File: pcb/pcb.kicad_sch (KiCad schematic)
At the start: 0 parts

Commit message: Start the schematic for the PCB
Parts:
- added J1: Conn_01x04_Pin, symbol Connector:Conn_01x04_Pin
- added J2: Conn_01x06_Pin, symbol Connector:Conn_01x06_Pin
- added R1, R10, R11, R12, R13, R14, R15, R16, R2, R3, R4, R5, R6, R7, R8, R9: 10k, symbol Device:R
- added U1: XIAO-ESP32-C5-DIP, Seeed_Studio_XIAO_Series:XIAO-ESP32-C5-DIP, symbol XIAO_Symbols:XIAO-ESP32-C5-DIP
- added U16: (no value), symbol esp32_wroom:esp32-s3-devkitc-1
- added U17: AP2112K-3.3, Package_TO_SOT_SMD:SOT-23-5, symbol Regulator_Linear:AP2112K-3.3
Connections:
- new net +5V: U1.14 (VBUS), U16.21 (5V)
- new net GND: U1.13 (GND), U16.22 (GND)
- new net MISO: U1.10 (GPIO9_D9_MISO), U16.19 (GPIO13)
- new net MOSI: U1.11 (GPIO18_D10_MOSI), U16.17 (GPIO11)
- new net SCK: J2.2 (Pin_2), U1.9 (GPIO8_D8_SCK), U16.18 (GPIO12)
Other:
- note added: "3.3V"
- note added: "5V"
- note added: "CS"
- note added: "GND"
- note added: "MISO"
- note added: "MOSI"
- note added: "RX"
- note added: "SCLK"
- note added: "TX"
- title: (none) -> wifydra-spi

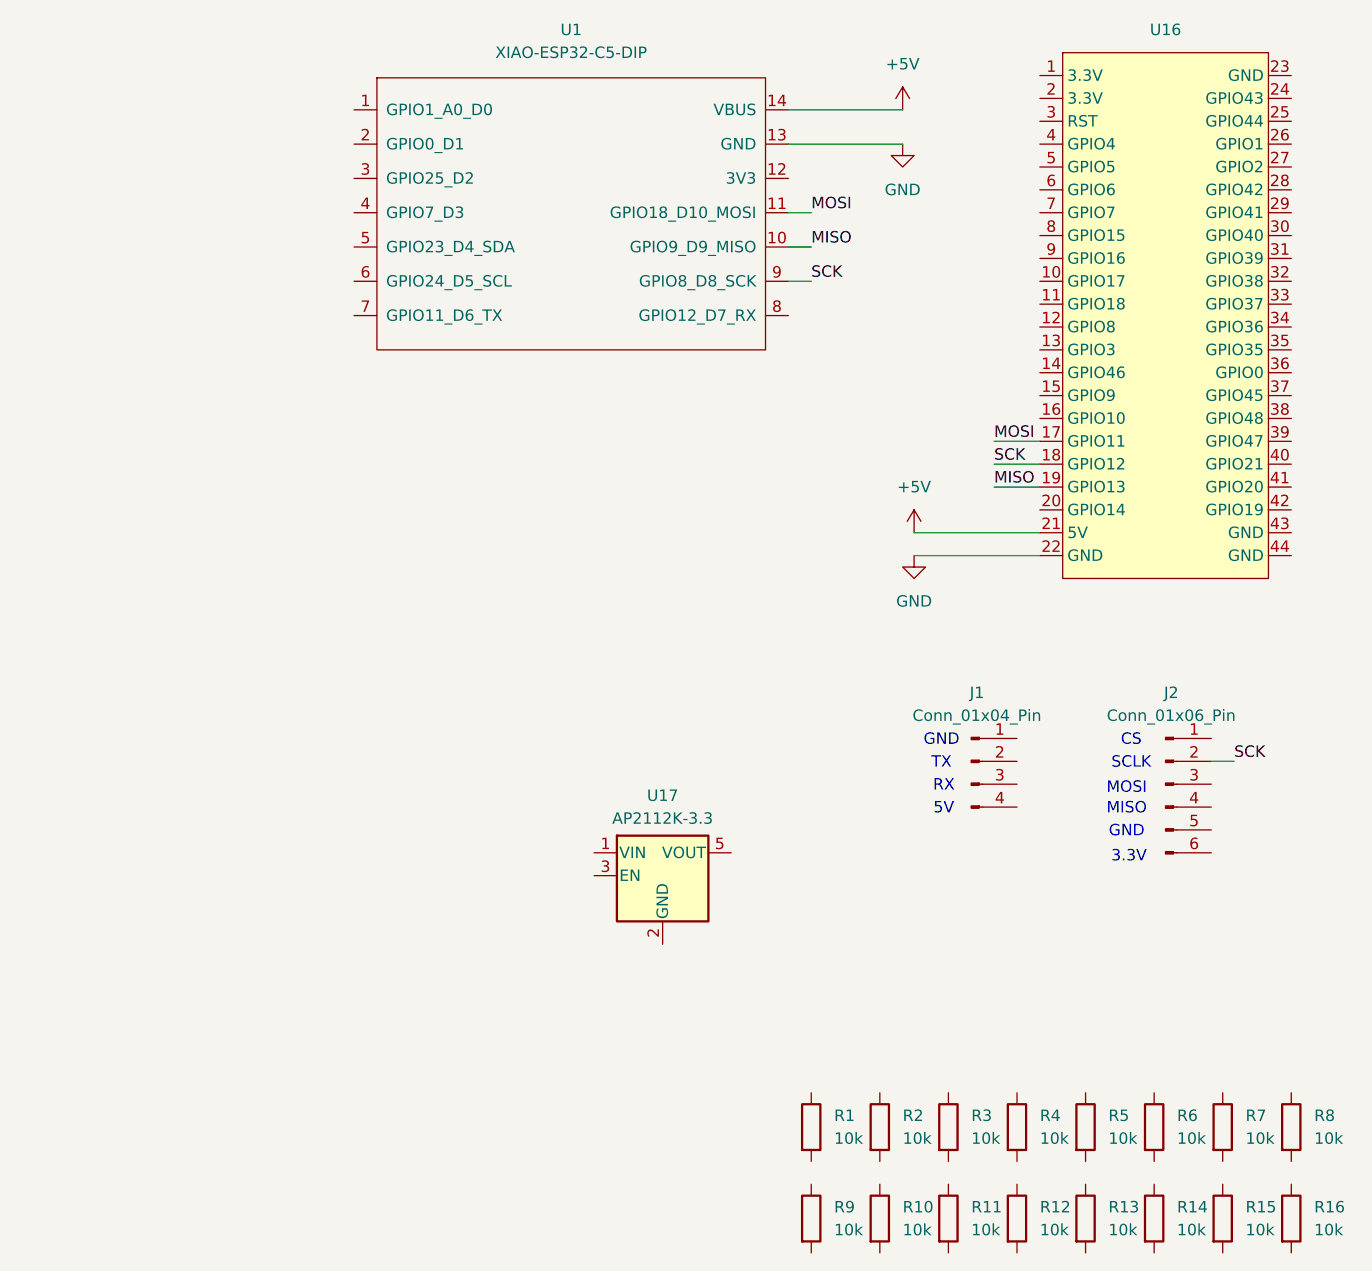
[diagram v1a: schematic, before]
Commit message: More wiring on the PCB design
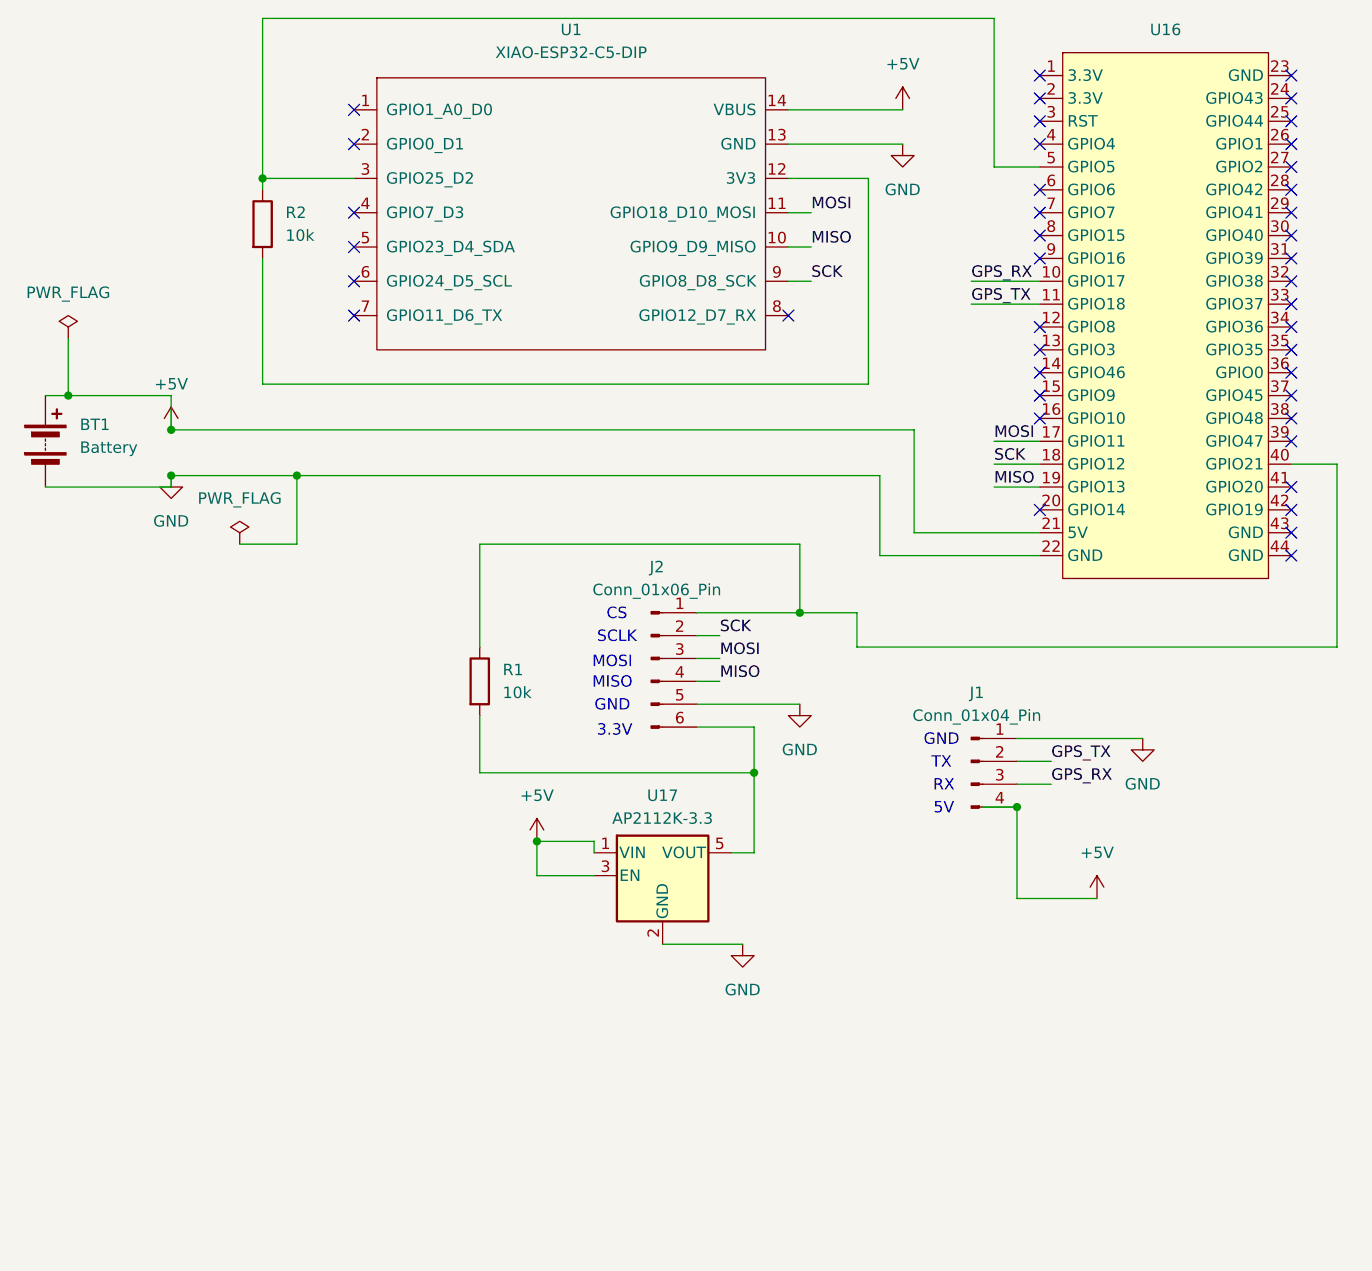
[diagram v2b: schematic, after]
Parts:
- removed R10, R11, R12, R13, R14, R15, R16, R3, R4, R5, R6, R7, R8, R9: 10k, symbol Device:R
- added BT1: Battery, Connector_PinHeader_2.54mm:PinHeader_1x02_P2.54mm_Horizontal, symbol Device:Battery
- J1: footprint (none) -> Connector_PinHeader_2.54mm:PinHeader_1x04_P2.54mm_Horizontal
- J2: footprint (none) -> Connector_PinHeader_2.54mm:PinHeader_1x06_P2.54mm_Vertical
- R1, R2: footprint (none) -> Resistor_THT:R_Axial_DIN0204_L3.6mm_D1.6mm_P5.08mm_Horizontal
- U1: footprint Seeed_Studio_XIAO_Series:XIAO-ESP32-C5-DIP -> xiao_footprints:XIAO-ESP32-C5-DIP
- U16: footprint (none) -> PCM_Espressif:ESP32-S3-DevKitC
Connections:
- net +5V: now also J1.4 (Pin_4), U17.1 (VIN), U17.3 (EN), BT1.1 (+)
- net GND: now also J1.1 (Pin_1), J2.5 (Pin_5), U17.2 (GND), BT1.2 (-)
- net MISO: now also J2.4 (Pin_4)
- net MOSI: now also J2.3 (Pin_3)
- net GPS_TX: now reaches J1.2 (Pin_2)
- net GPS_TX: now also U16.11 (GPIO18)
- net GPS_RX: now reaches J1.3 (Pin_3)
- net GPS_RX: now also U16.10 (GPIO17)
- net at R1.1: now also J2.1 (Pin_1), U16.40 (GPIO21)
- net at R1.2: now also J2.6 (Pin_6), U17.5 (VOUT)
- net at U16.5 (GPIO5): now also R2.1, U1.3 (GPIO25_D2)
- net at R2.2: now also U1.12 (3V3)
- no-connect marks 0 -> 42
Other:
- moved on the sheet: J2, R1, R2

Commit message: tidy schematic
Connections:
- net GND: now also U16.44 (GND)
- net at J2.1 (Pin_1), R1.1, U16.40 (GPIO21): now also J2.6 (Pin_6), R1.2, U17.5 (VOUT)
- net at R2.1, U1.3 (GPIO25_D2), U16.5 (GPIO5): now also R2.2, U1.12 (3V3)
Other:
- moved on the sheet: BT1, J2, R1, R2, U1, U16, U17

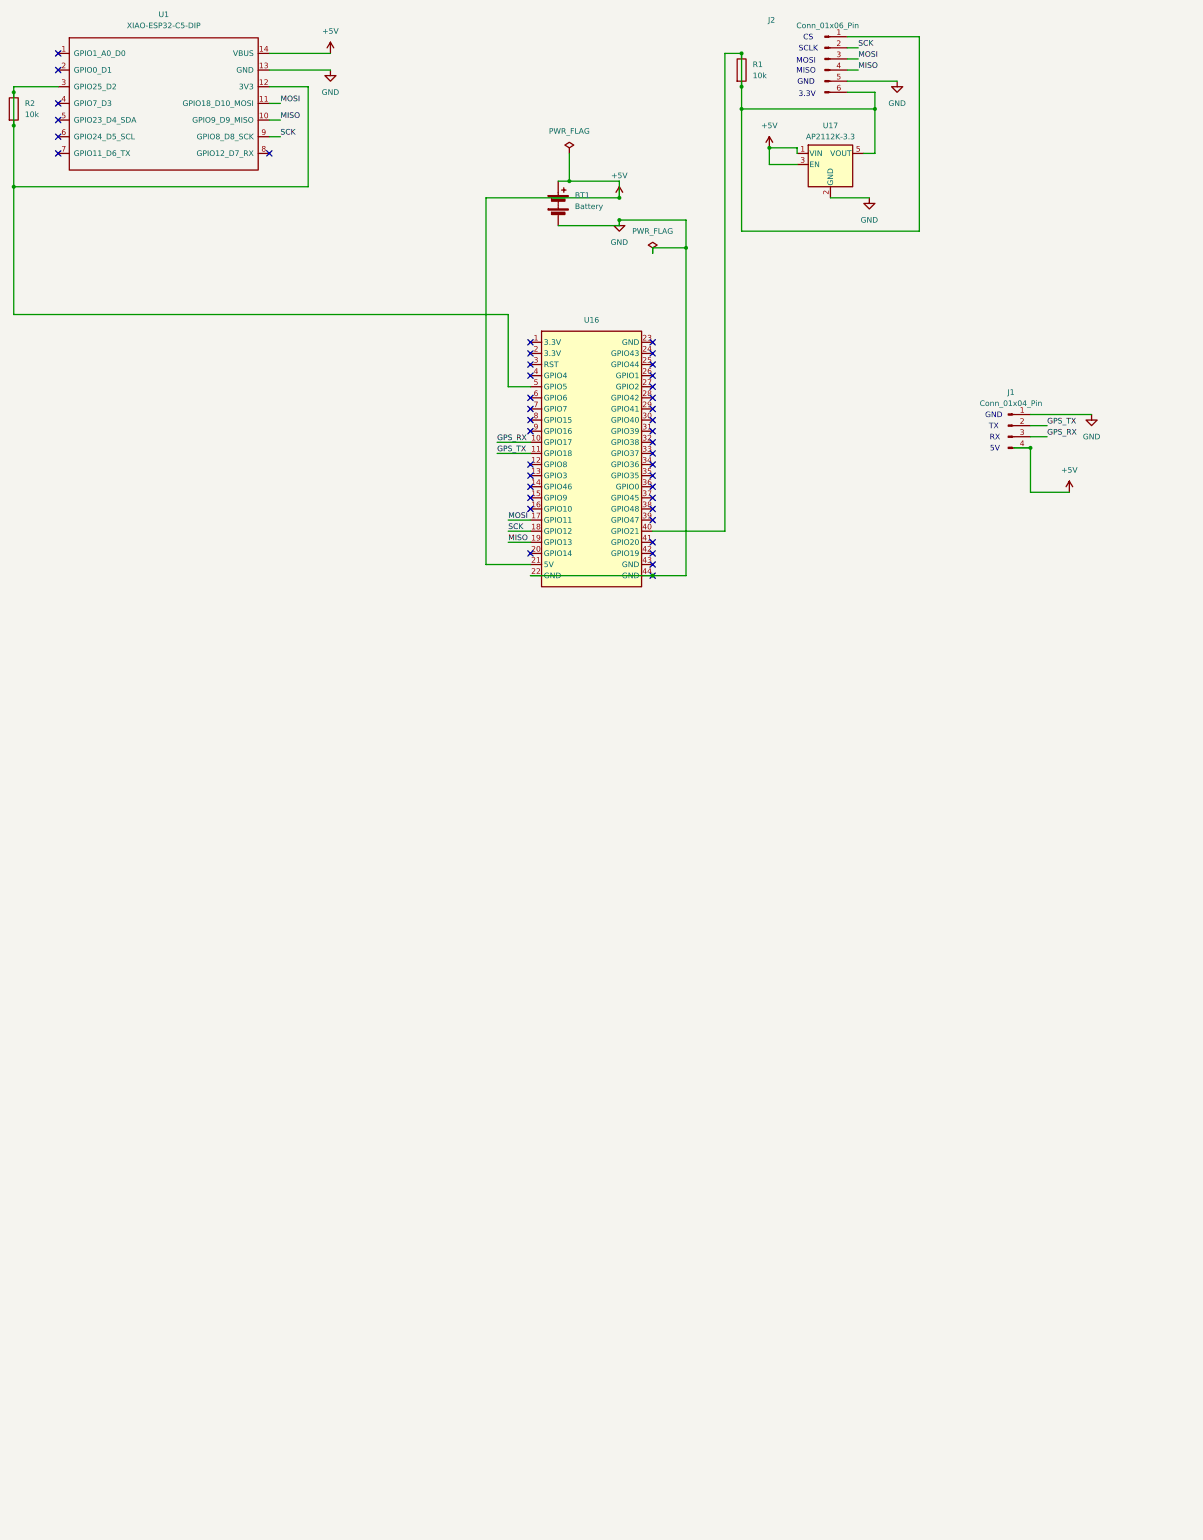
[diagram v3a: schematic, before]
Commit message: Increase worker count to 16, wire up the PCB
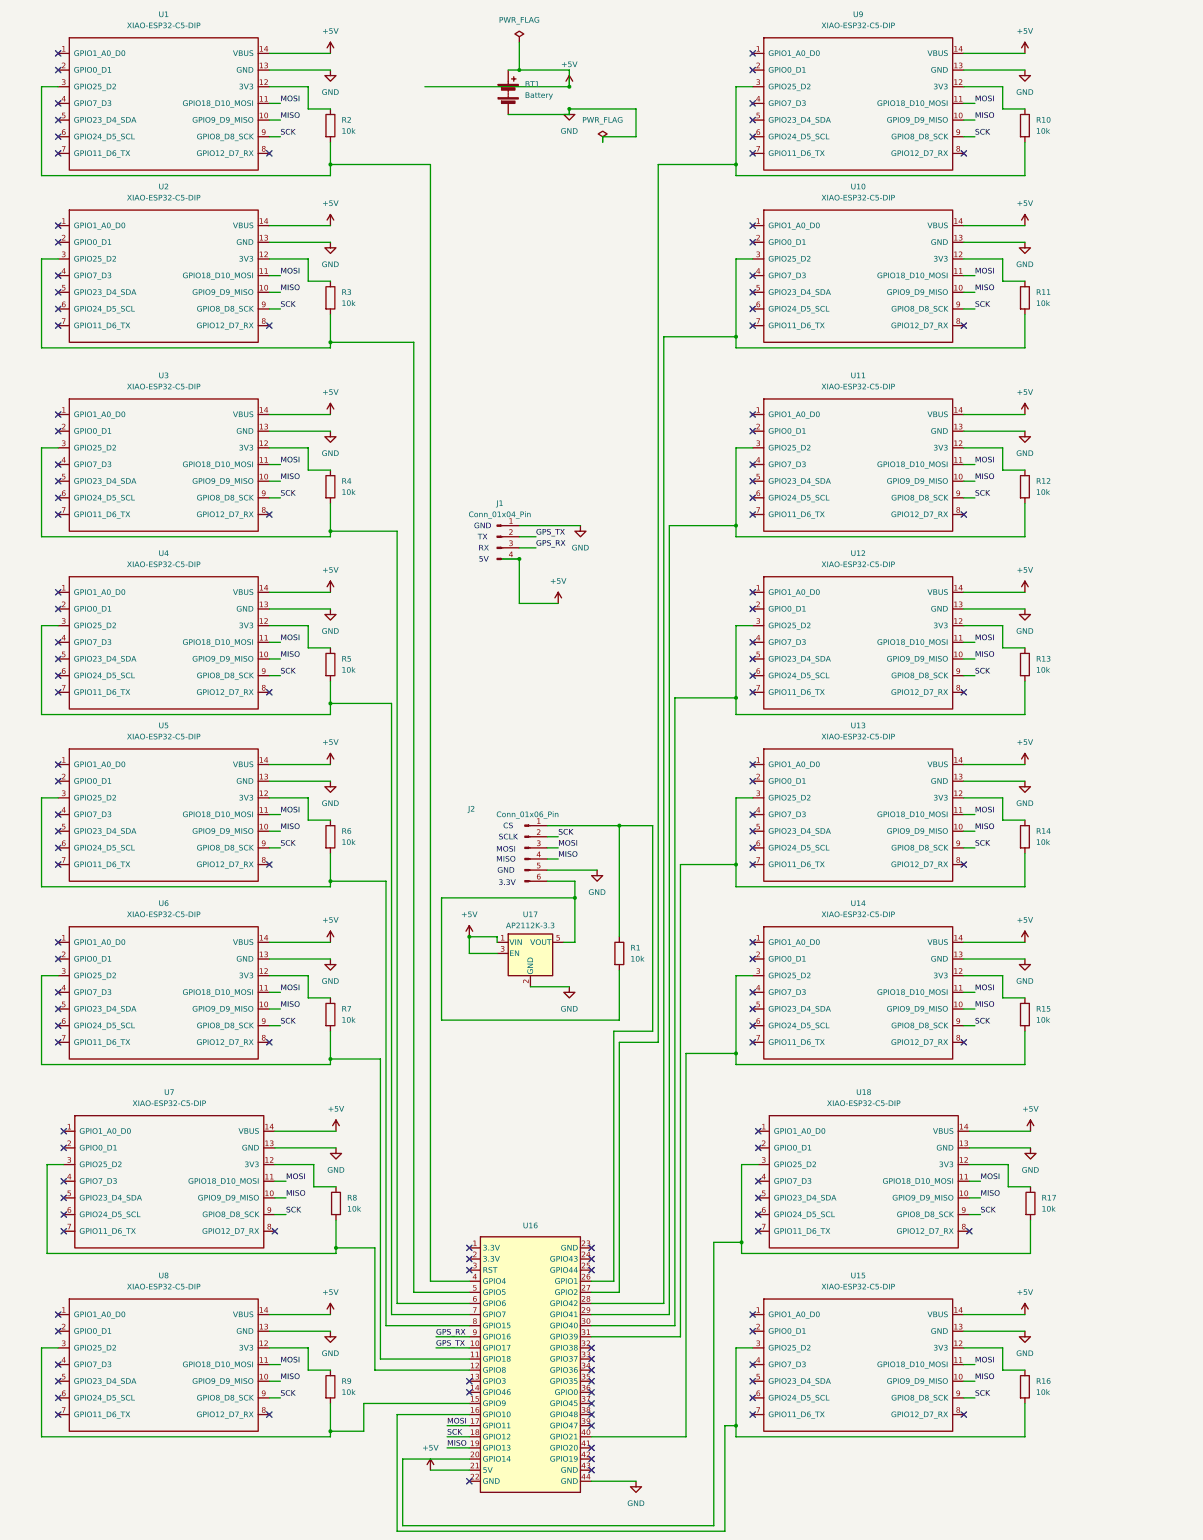
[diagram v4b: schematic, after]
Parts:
- added R10, R11, R12, R13, R14, R15, R16, R17, R3, R4, R5, R6, R7, R8, R9: 10k, Resistor_THT:R_Axial_DIN0204_L3.6mm_D1.6mm_P5.08mm_Horizontal, symbol Device:R
- added U10, U11, U12, U13, U14, U15, U18, U2, U3, U4, U5, U6, U7, U8, U9: XIAO-ESP32-C5-DIP, xiao_footprints:XIAO-ESP32-C5-DIP, symbol XIAO_Symbols:XIAO-ESP32-C5-DIP
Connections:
- net +5V: now also U10.14 (VBUS), U11.14 (VBUS), U12.14 (VBUS), U13.14 (VBUS), U14.14 (VBUS), U15.14 (VBUS), U18.14 (VBUS), U2.14 (VBUS), U3.14 (VBUS), U4.14 (VBUS), U5.14 (VBUS), U6.14 (VBUS), U7.14 (VBUS), U8.14 (VBUS), U9.14 (VBUS)
- net GND: now also U10.13 (GND), U11.13 (GND), U12.13 (GND), U13.13 (GND), U14.13 (GND), U15.13 (GND), U18.13 (GND), U2.13 (GND), U3.13 (GND), U4.13 (GND), U5.13 (GND), U6.13 (GND), U7.13 (GND), U8.13 (GND), U9.13 (GND); no longer U16.22 (GND)
- net GPS_RX: now also U16.9 (GPIO16); no longer U16.10 (GPIO17)
- net GPS_TX: now also U16.10 (GPIO17); no longer U16.11 (GPIO18)
- net MISO: now also U10.10 (GPIO9_D9_MISO), U11.10 (GPIO9_D9_MISO), U12.10 (GPIO9_D9_MISO), U13.10 (GPIO9_D9_MISO), U14.10 (GPIO9_D9_MISO), U15.10 (GPIO9_D9_MISO), U18.10 (GPIO9_D9_MISO), U2.10 (GPIO9_D9_MISO), U3.10 (GPIO9_D9_MISO), U4.10 (GPIO9_D9_MISO), U5.10 (GPIO9_D9_MISO), U6.10 (GPIO9_D9_MISO), U7.10 (GPIO9_D9_MISO), U8.10 (GPIO9_D9_MISO), U9.10 (GPIO9_D9_MISO)
- net MOSI: now also U10.11 (GPIO18_D10_MOSI), U11.11 (GPIO18_D10_MOSI), U12.11 (GPIO18_D10_MOSI), U13.11 (GPIO18_D10_MOSI), U14.11 (GPIO18_D10_MOSI), U15.11 (GPIO18_D10_MOSI), U18.11 (GPIO18_D10_MOSI), U2.11 (GPIO18_D10_MOSI), U3.11 (GPIO18_D10_MOSI), U4.11 (GPIO18_D10_MOSI), U5.11 (GPIO18_D10_MOSI), U6.11 (GPIO18_D10_MOSI), U7.11 (GPIO18_D10_MOSI), U8.11 (GPIO18_D10_MOSI), U9.11 (GPIO18_D10_MOSI)
- net SCK: now also U10.9 (GPIO8_D8_SCK), U11.9 (GPIO8_D8_SCK), U12.9 (GPIO8_D8_SCK), U13.9 (GPIO8_D8_SCK), U14.9 (GPIO8_D8_SCK), U15.9 (GPIO8_D8_SCK), U18.9 (GPIO8_D8_SCK), U2.9 (GPIO8_D8_SCK), U3.9 (GPIO8_D8_SCK), U4.9 (GPIO8_D8_SCK), U5.9 (GPIO8_D8_SCK), U6.9 (GPIO8_D8_SCK), U7.9 (GPIO8_D8_SCK), U8.9 (GPIO8_D8_SCK), U9.9 (GPIO8_D8_SCK)
- net at J2.6 (Pin_6), R1.2, U17.5 (VOUT): no longer J2.1 (Pin_1), R1.1, U16.40 (GPIO21)
- net at U16.12 (GPIO8): now also R8.2, U7.3 (GPIO25_D2)
- net at U16.15 (GPIO9): now also R9.2, U8.3 (GPIO25_D2)
- net at U16.16 (GPIO10): now also R16.2, U15.3 (GPIO25_D2)
- net at U16.20 (GPIO14): now also R17.2, U18.3 (GPIO25_D2)
- net at U16.26 (GPIO1): now also J2.1 (Pin_1), R1.1
- net at U16.27 (GPIO2): now also R10.2, U9.3 (GPIO25_D2)
- net at U16.28 (GPIO42): now also R11.2, U10.3 (GPIO25_D2)
- net at U16.29 (GPIO41): now also R12.2, U11.3 (GPIO25_D2)
- net at U16.30 (GPIO40): now also R13.2, U12.3 (GPIO25_D2)
- net at U16.31 (GPIO39): now also R14.2, U13.3 (GPIO25_D2)
- net at U16.4 (GPIO4): now also R2.2, U1.3 (GPIO25_D2)
- net at U16.6 (GPIO6): now also R4.2, U3.3 (GPIO25_D2)
- net at U16.7 (GPIO7): now also R5.2, U4.3 (GPIO25_D2)
- net at U16.8 (GPIO15): now also R6.2, U5.3 (GPIO25_D2)
- new net: R4.1, U3.12 (3V3)
- new net: R12.1, U11.12 (3V3)
- new net: R15.1, U14.12 (3V3)
- new net: R15.2, U14.3 (GPIO25_D2), U16.40 (GPIO21)
- new net: R10.1, U9.12 (3V3)
- new net: R7.1, U6.12 (3V3)
- new net: R7.2, U16.11 (GPIO18), U6.3 (GPIO25_D2)
- new net: R13.1, U12.12 (3V3)
- new net: R3.1, U2.12 (3V3)
- new net: R3.2, U16.5 (GPIO5), U2.3 (GPIO25_D2)
- new net: R11.1, U10.12 (3V3)
- new net: R16.1, U15.12 (3V3)
- new net: R14.1, U13.12 (3V3)
- new net: R6.1, U5.12 (3V3)
- new net: R8.1, U7.12 (3V3)
- new net: R5.1, U4.12 (3V3)
- new net: R9.1, U8.12 (3V3)
- new net: R17.1, U18.12 (3V3)
- new net: R2.1, U1.12 (3V3)
- no-connect marks 42 -> 132
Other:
- moved on the sheet: BT1, J1, J2, R1, R2, U16, U17

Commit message: tidy up warnings
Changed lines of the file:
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@@
 	)
 	(junction
-		(at 130.81 138.43)
-		(diameter 0)
-		(color 0 0 0 0)
-	)
-	(junction
-		(at 142.24 30.48)
-		(diameter 0)
-		(color 0 0 0 0)
-	)
-	(junction
 		(at 87.63 252.73)
 		(diameter 0)
@@
 	(wire
 		(pts
-			(xy 127 138.43) (xy 130.81 138.43)
-		)
-		(stroke
-			(width 0)
-			(type default)
-		)
-	)
-	(wire
-		(pts
 			(xy 143.51 226.06) (xy 140.97 226.06)
 		)
@@
 	(wire
 		(pts
-			(xy 157.48 35.56) (xy 157.48 41.91)
+			(xy 157.48 35.56) (xy 157.48 43.18)
 		)
 		(stroke
@@
 	(wire
 		(pts
-			(xy 157.48 41.91) (xy 149.86 41.91)
+			(xy 157.48 43.18) (xy 149.86 43.18)
 		)
 		(stroke
@@
 	(wire
 		(pts
-			(xy 142.24 30.48) (xy 109.22 30.48)
-		)
-		(stroke
-			(width 0)
-			(type default)
-		)
-	)
-	(wire
-		(pts
 			(xy 153.67 248.92) (xy 162.56 248.92)
 		)
@@
 	(wire
 		(pts
-			(xy 149.86 41.91) (xy 149.86 43.18)
-		)
-		(stroke
-			(width 0)
-			(type default)
-		)
-	)
-	(wire
-		(pts
 			(xy 99.06 321.31) (xy 119.38 321.31)
 		)
@@
 	(wire
 		(pts
-			(xy 142.24 26.67) (xy 142.24 30.48)
+			(xy 142.24 26.67) (xy 142.24 25.4)
 		)
 		(stroke
@@
 	(symbol
 		(lib_id "power:+5V")
-		(at 142.24 30.48 0)
+		(at 142.24 25.4 0)
 		(unit 1)
 		(body_style 1)
@@
 		(fields_autoplaced yes)
 		(property "Reference" "#PWR01"
-			(at 142.24 34.29 0)
+			(at 142.24 29.21 0)
 			(hide yes)
 			(show_name no)
@@
 		)
 		(property "Value" "+5V"
-			(at 142.24 25.4 0)
+			(at 142.24 20.32 0)
 			(show_name no)
 			(do_not_autoplace no)
@@
 		)
 		(property "Footprint" ""
-			(at 142.24 30.48 0)
+			(at 142.24 25.4 0)
 			(hide yes)
 			(show_name no)
@@
 		)
 		(property "Datasheet" ""
-			(at 142.24 30.48 0)
+			(at 142.24 25.4 0)
 			(hide yes)
 			(show_name no)
@@
 		)
 		(property "Description" "Power symbol creates a global label with name \"+5V\""
-			(at 142.24 30.48 0)
+			(at 142.24 25.4 0)
 			(hide yes)
 			(show_name no)
